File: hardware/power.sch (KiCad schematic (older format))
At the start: 23 parts, among them U5 BQ24210DQCT, U6 LTC1983ES6-3

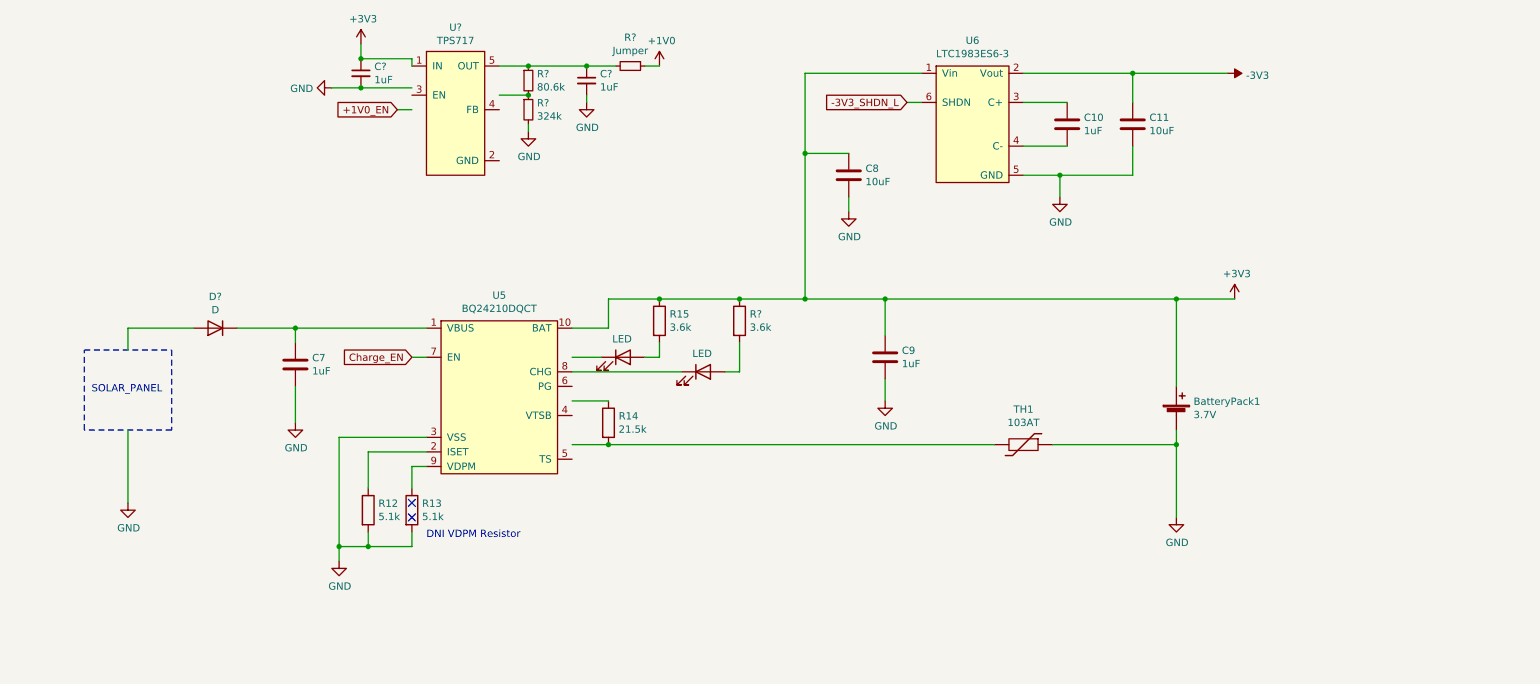
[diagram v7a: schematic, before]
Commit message: House Keeping Tasks
 - Modified parts list parameters for various parts
 - Assigned Ref Des to components
 - Changed TPS717 symbol and feedback resistors
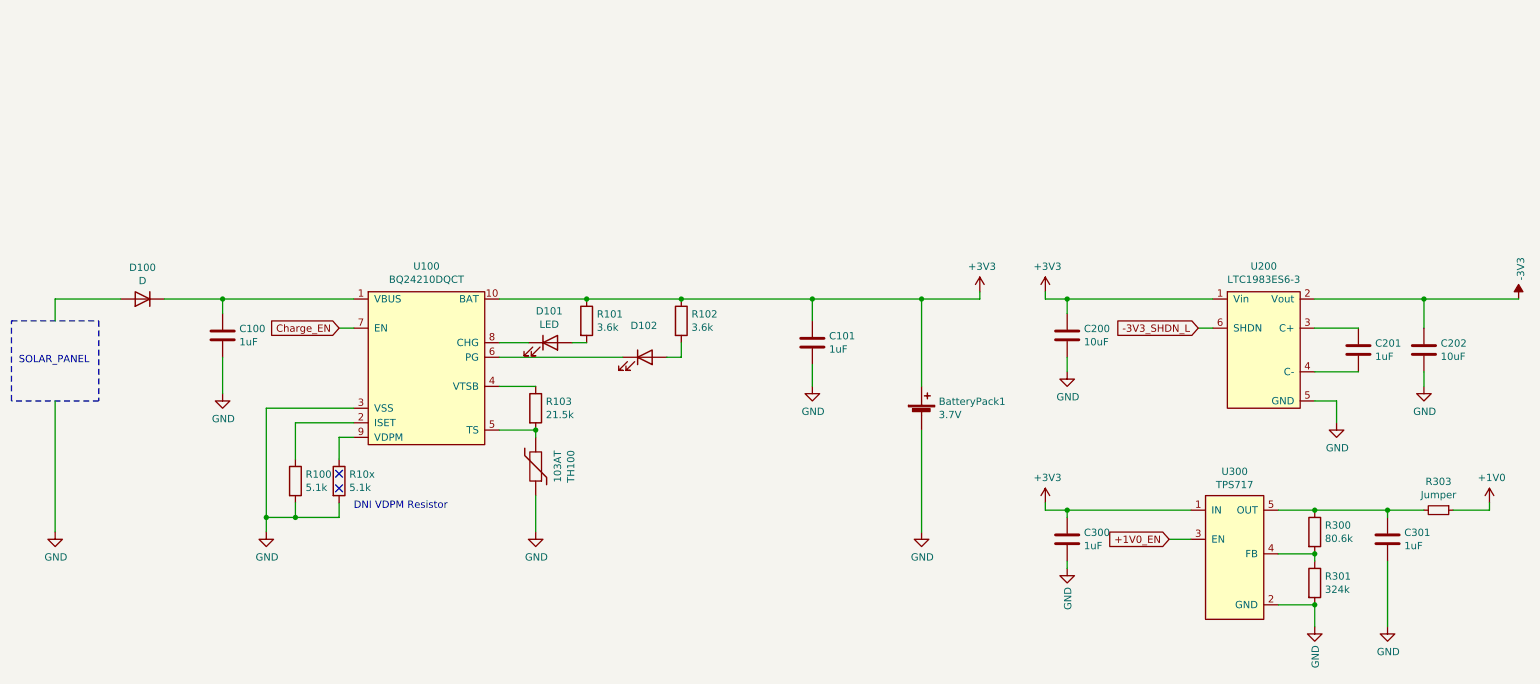
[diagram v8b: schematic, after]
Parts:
- removed C11: 10uF, symbol Device:C
- removed C7: 1uF, symbol Device:C
- removed C? (x2): 1uF, symbol Device:C_Small
- removed D2: LED, symbol Device:LED
- removed R13: 5.1k, symbol Device:R
- removed R?: 80.6k, symbol Device:R_Small
- removed R?: 324k, symbol Device:R_Small
- added C100, C300, C301: 1uF, Capacitor_SMD:C_0603_1608Metric_Pad1.08x0.95mm_HandSolder, symbol Device:C
- added C202: 10uF, Capacitor_SMD:C_0603_1608Metric_Pad1.08x0.95mm_HandSolder, symbol Device:C
- added D101: LED, LED_SMD:LED_0603_1608Metric_Pad1.05x0.95mm_HandSolder, symbol Device:LED
- added R10x: 5.1k, Resistor_SMD:R_0603_1608Metric_Pad0.98x0.95mm_HandSolder, symbol Device:R
- added R300: 80.6k, Resistor_SMD:R_0603_1608Metric_Pad0.98x0.95mm_HandSolder, symbol Device:R
- added R301: 324k, Resistor_SMD:R_0603_1608Metric_Pad0.98x0.95mm_HandSolder, symbol Device:R
- C101: renamed from C9; footprint (none) -> Capacitor_SMD:C_0603_1608Metric_Pad1.08x0.95mm_HandSolder
- C200: renamed from C8; footprint (none) -> Capacitor_SMD:C_0603_1608Metric_Pad1.08x0.95mm_HandSolder
- D100: renamed from D?; footprint (none) -> Diode_SMD:D_SMA_Handsoldering; Digikey (none) -> S1B-13-F
- D102: renamed from D3; footprint (none) -> LED_SMD:LED_0603_1608Metric_Pad1.05x0.95mm_HandSolder; Digikey (none) -> 1497-1215-1-ND
- R100: renamed from R12; footprint (none) -> Resistor_SMD:R_0603_1608Metric_Pad0.98x0.95mm_HandSolder
- R101: renamed from R15; footprint (none) -> Resistor_SMD:R_0603_1608Metric_Pad0.98x0.95mm_HandSolder
- R102, R303: renamed from R?; footprint (none) -> Resistor_SMD:R_0603_1608Metric_Pad0.98x0.95mm_HandSolder
- R103: renamed from R14; footprint (none) -> Resistor_SMD:R_0603_1608Metric_Pad0.98x0.95mm_HandSolder
- gave numbers to parts that had none: 1
- renumbered C10 to C201, TH1 to TH100, U5 to U100, U6 to U200
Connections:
- wire segments 70 -> 69
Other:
- moved on the sheet: BatteryPack1, C101, C200, C201, D100, R100, R101, R102, R103, R303, TH100, U100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
